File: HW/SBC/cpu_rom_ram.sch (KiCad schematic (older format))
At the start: 3 parts, among them U1 WD65C02_, U2 28C256, U3 HM62256BLP-7

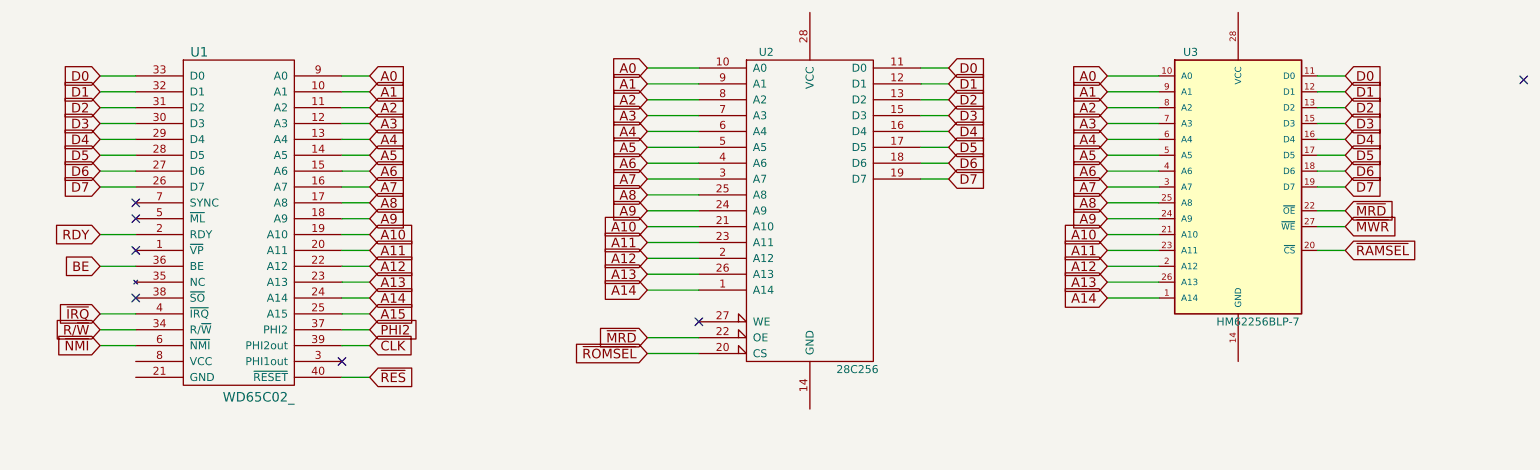
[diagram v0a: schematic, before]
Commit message: Move dicoupling capacitators as close the chips as possible.
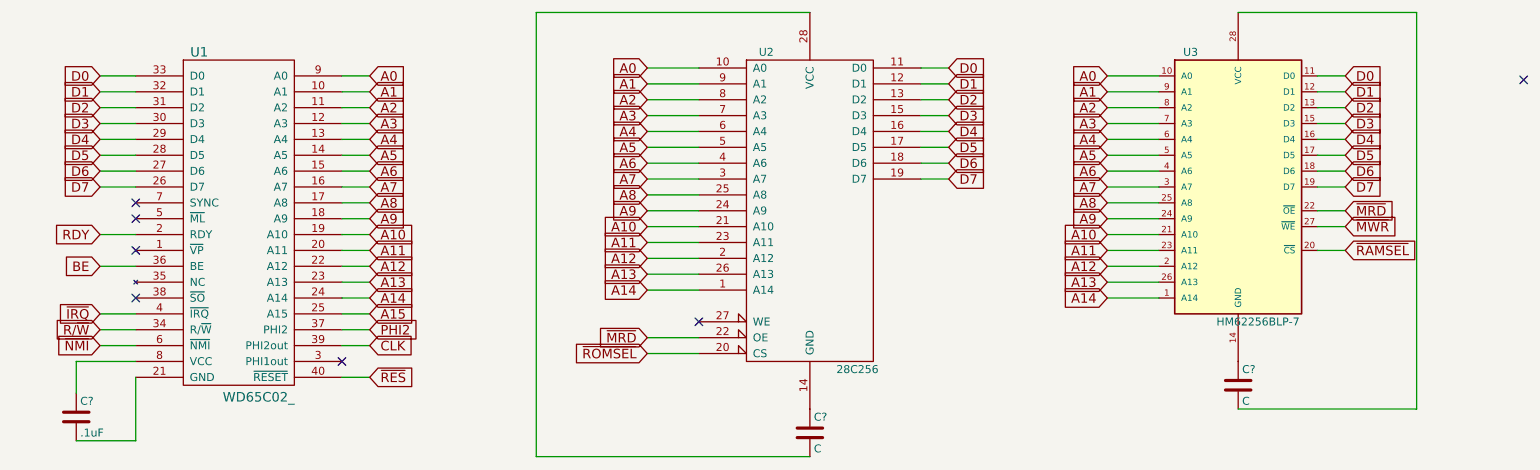
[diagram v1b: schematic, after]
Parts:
- added C?: .1uF, symbol C
- added C? (x2): C, symbol C
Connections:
- net at U1.21 (GND): now also C?.2
- net at U1.8 (VCC): now also C?.1
- net at U2.14 (GND): now also C?.1
- net at U2.28 (VCC): now also C?.2
- net at U3.14 (GND): now also C?.1
- net at U3.28 (VCC): now also C?.2
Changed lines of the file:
@@
 NoConn ~ 5075 3000
 NoConn ~ 10275 1475
+$Comp
+L C C?
+U 1 1 59051EFC
+P 1150 3600
+F 0 "C?" H 1175 3700 50  0000 L CNN
+F 1 ".1uF" H 1175 3500 50  0000 L CNN
+F 2 "" H 1188 3450 50  0001 C CNN
+F 3 "" H 1150 3600 50  0001 C CNN
+	1    1150 3600
+	1    0    0    -1
+$EndComp
+Wire Wire Line
+	1150 3450 1150 3250
+Wire Wire Line
+	1150 3250 1525 3250
+Wire Wire Line
+	1150 3750 1525 3750
+Wire Wire Line
+	1525 3750 1525 3350
+$Comp
+L C C?
+U 1 1 59052A5B
+P 5775 3700
+F 0 "C?" H 5800 3800 50  0000 L CNN
+F 1 "C" H 5800 3600 50  0000 L CNN
+F 2 "" H 5813 3550 50  0001 C CNN
+F 3 "" H 5775 3700 50  0001 C CNN
+	1    5775 3700
+	1    0    0    -1
+$EndComp
+Wire Wire Line
+	5775 3850 4050 3850
+Wire Wire Line
+	4050 3850 4050 1050
+Wire Wire Line
+	4050 1050 5775 1050
+$Comp
+L C C?
+U 1 1 59052F49
+P 8475 3400
+F 0 "C?" H 8500 3500 50  0000 L CNN
+F 1 "C" H 8500 3300 50  0000 L CNN
+F 2 "" H 8513 3250 50  0001 C CNN
+F 3 "" H 8475 3400 50  0001 C CNN
+	1    8475 3400
+	1    0    0    -1
+$EndComp
+Wire Wire Line
+	8475 3550 9600 3550
+Wire Wire Line
+	9600 3550 9600 1050
+Wire Wire Line
+	9600 1050 8475 1050
 $EndSCHEMATC

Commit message: Schema changes to SBC
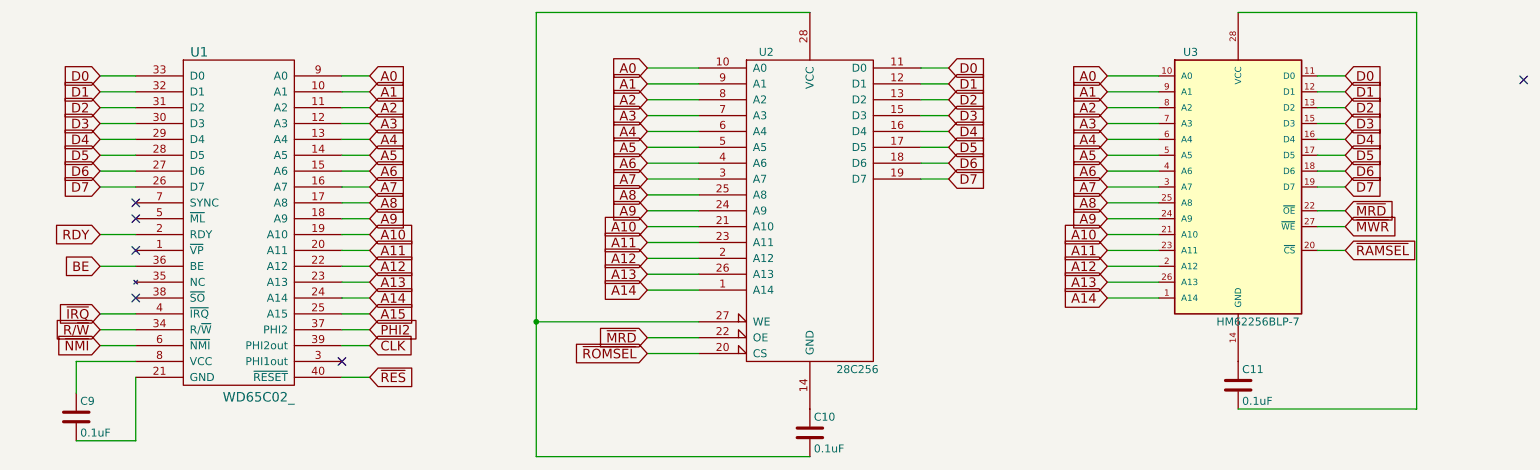
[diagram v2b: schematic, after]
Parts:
- C10, C11: renamed from C?; value C -> 0.1uF; footprint (none) -> Capacitors_ThroughHole:C_Disc_D3.8mm_W2.6mm_P2.50mm
- C9: renamed from C?; value .1uF -> 0.1uF; footprint (none) -> Capacitors_ThroughHole:C_Disc_D3.8mm_W2.6mm_P2.50mm
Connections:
- net at U2.27 (WE): now also C10.2, U2.28 (VCC)
- no-connect marks 7 -> 6
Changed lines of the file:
@@
 Text GLabel 4750 3200 0    60   Input ~ 0
 ~ROMSEL
-NoConn ~ 5075 3000
 NoConn ~ 10275 1475
 $Comp
-L C C?
+L C C9
 U 1 1 59051EFC
 P 1150 3600
-F 0 "C?" H 1175 3700 50  0000 L CNN
-F 1 ".1uF" H 1175 3500 50  0000 L CNN
-F 2 "" H 1188 3450 50  0001 C CNN
+F 0 "C9" H 1175 3700 50  0000 L CNN
+F 1 "0.1uF" H 1175 3500 50  0000 L CNN
+F 2 "Capacitors_ThroughHole:C_Disc_D3.8mm_W2.6mm_P2.50mm" H 1188 3450 50  0001 C CNN
 F 3 "" H 1150 3600 50  0001 C CNN
 	1    1150 3600
@@
 	1525 3750 1525 3350
 $Comp
-L C C?
+L C C10
 U 1 1 59052A5B
 P 5775 3700
-F 0 "C?" H 5800 3800 50  0000 L CNN
-F 1 "C" H 5800 3600 50  0000 L CNN
-F 2 "" H 5813 3550 50  0001 C CNN
+F 0 "C10" H 5800 3800 50  0000 L CNN
+F 1 "0.1uF" H 5800 3600 50  0000 L CNN
+F 2 "Capacitors_ThroughHole:C_Disc_D3.8mm_W2.6mm_P2.50mm" H 5813 3550 50  0001 C CNN
 F 3 "" H 5775 3700 50  0001 C CNN
 	1    5775 3700
@@
 	4050 1050 5775 1050
 $Comp
-L C C?
+L C C11
 U 1 1 59052F49
 P 8475 3400
-F 0 "C?" H 8500 3500 50  0000 L CNN
-F 1 "C" H 8500 3300 50  0000 L CNN
-F 2 "" H 8513 3250 50  0001 C CNN
+F 0 "C11" H 8500 3500 50  0000 L CNN
+F 1 "0.1uF" H 8500 3300 50  0000 L CNN
+F 2 "Capacitors_ThroughHole:C_Disc_D3.8mm_W2.6mm_P2.50mm" H 8513 3250 50  0001 C CNN
 F 3 "" H 8475 3400 50  0001 C CNN
 	1    8475 3400
@@
 Wire Wire Line
 	9600 1050 8475 1050
+Wire Wire Line
+	5075 3000 4050 3000
+Connection ~ 4050 3000
 $EndSCHEMATC
